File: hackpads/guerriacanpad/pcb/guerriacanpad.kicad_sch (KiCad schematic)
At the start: 53 parts, among them SW1 RotaryEncoder_Switch_MP, SW2 RotaryEncoder_Switch_MP, U1 Seeeduino Xiao rp2040, U2 MCP23008-xSO, U3 74AHC1G125

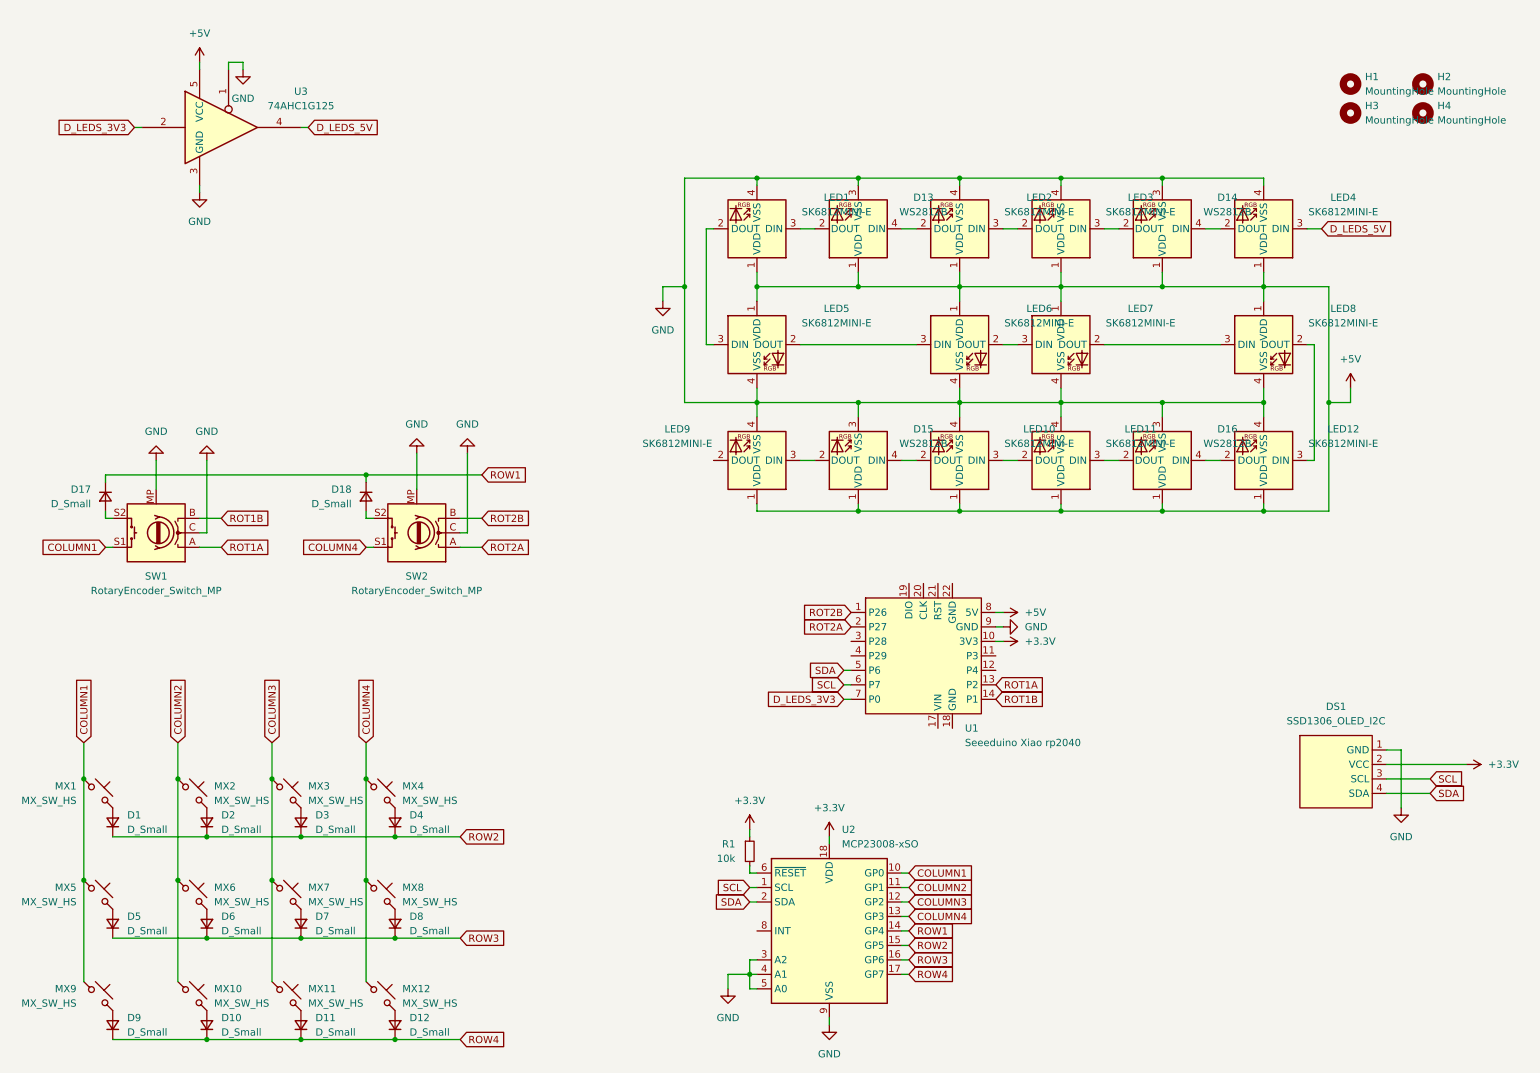
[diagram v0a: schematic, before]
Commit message: Changed the IO expander
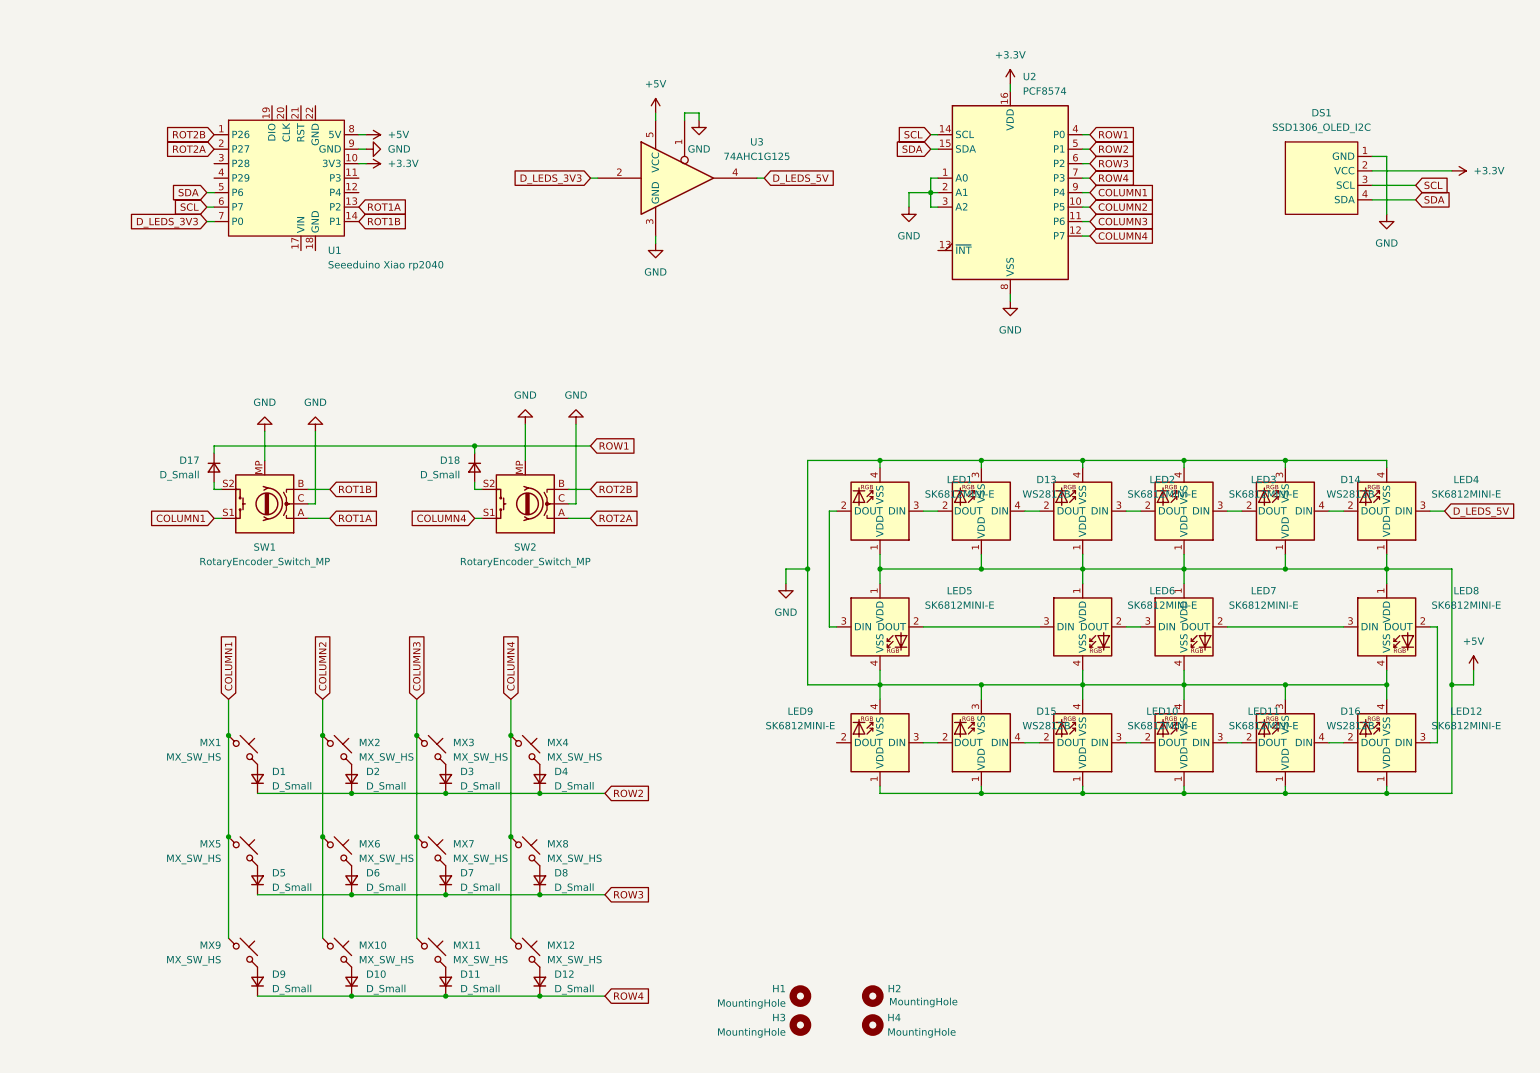
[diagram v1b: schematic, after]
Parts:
- removed R1: 10k, Resistor_SMD:R_0603_1608Metric_Pad0.98x0.95mm_HandSolder, symbol Device:R_Small
- removed U2: MCP23008-xSO, Package_SO:SOIC-18W_7.5x11.6mm_P1.27mm, symbol Interface_Expansion:MCP23008-xSO
- added U2: PCF8574, Package_SO:SOIC-16W_7.5x10.3mm_P1.27mm, symbol Interface_Expansion:PCF8574
- U3: footprint Package_TO_SOT_SMD:SOT-23-5_HandSoldering -> Package_TO_SOT_SMD:SOT-353_SC-70-5_Handsoldering
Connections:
- net +3.3V: now also U2.16 (VDD)
- net COLUMN1: now also U2.9 (P4)
- net COLUMN2: now also U2.10 (P5)
- net COLUMN3: now also U2.11 (P6)
- net COLUMN4: now also U2.12 (P7)
- net GND: now also U2.1 (A0), U2.2 (A1), U2.3 (A2), U2.8 (VSS)
- net ROW1: now also U2.4 (P0)
- net ROW2: now also U2.5 (P1)
- net ROW3: now also U2.6 (P2)
- net ROW4: now also U2.7 (P3)
- net SCL: now also U2.14 (SCL)
- net SDA: now also U2.15 (SDA)
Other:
- moved on the sheet: D1, D10, D11, D12, D13, D14, D15, D16, D17, D18, D2, D3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

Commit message: Added decoupling capacitors
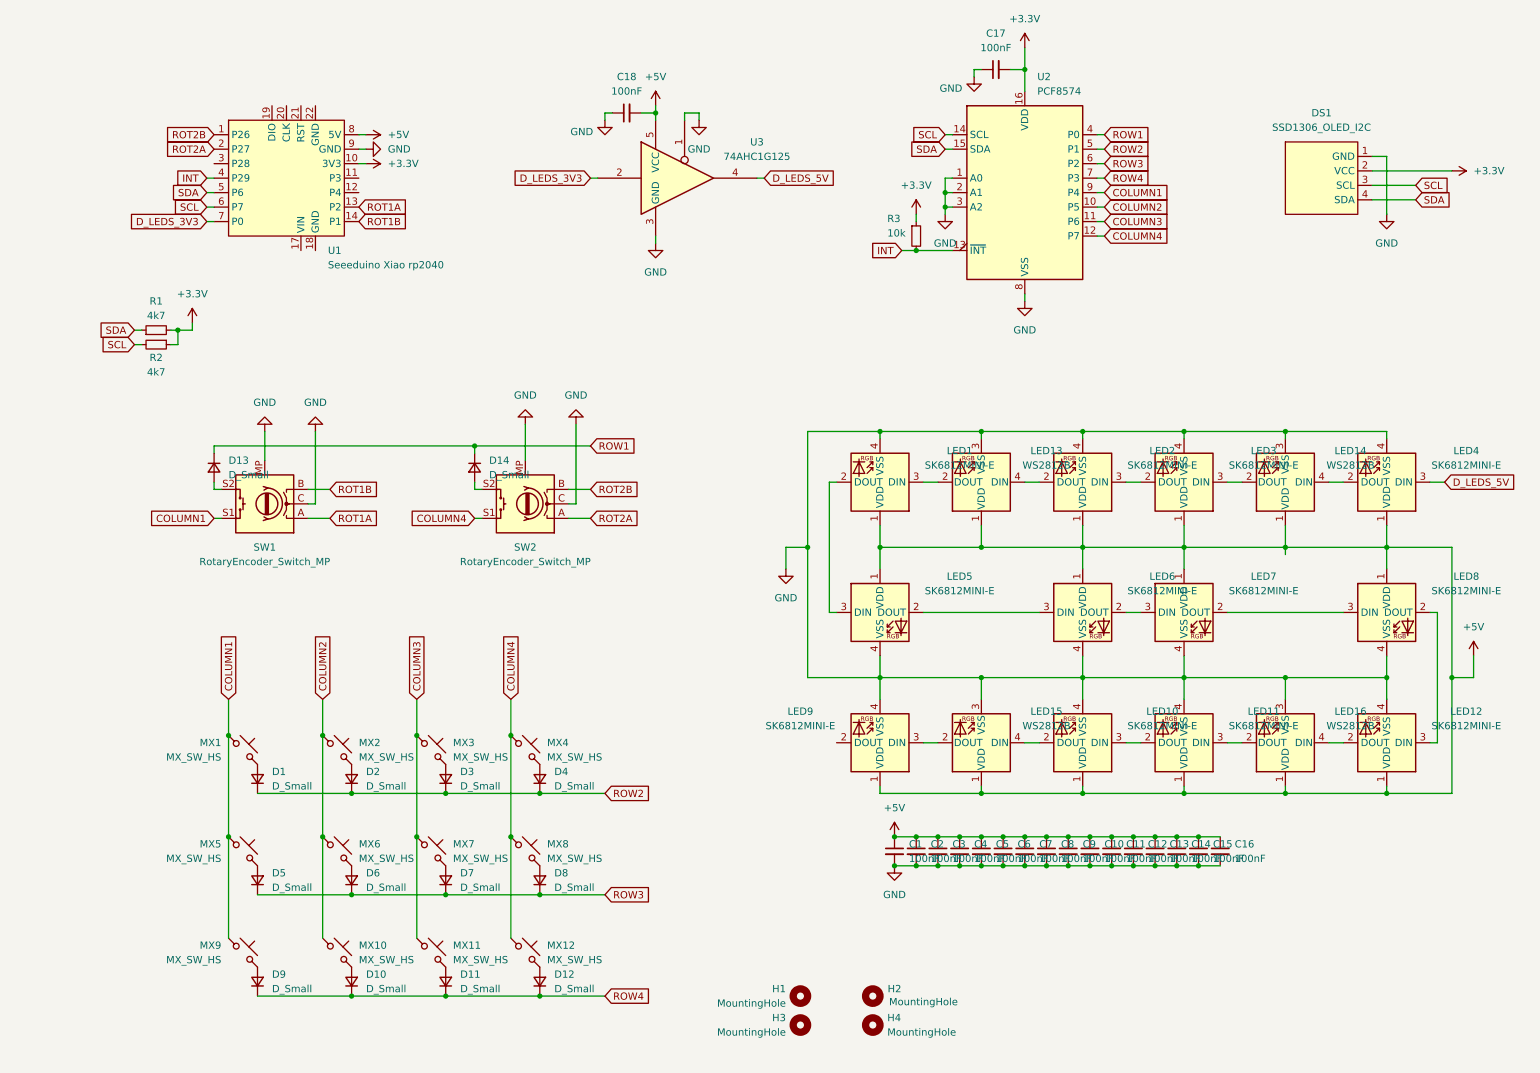
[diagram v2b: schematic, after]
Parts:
- added C1, C10, C11, C12, C13, C14, C15, C16, C17, C18, C2, C3, C4, C5, C6, C7, C8, C9: 100nF, Capacitor_SMD:C_0603_1608Metric_Pad1.08x0.95mm_HandSolder, symbol Device:C_Small
- added R1, R2: 4k7, Resistor_SMD:R_0603_1608Metric_Pad0.98x0.95mm_HandSolder, symbol Device:R_Small
- added R3: 10k, Resistor_SMD:R_0603_1608Metric_Pad0.98x0.95mm_HandSolder, symbol Device:R_Small
- renumbered D17 to D13, D18 to D14, D13 to LED13, D14 to LED14, D15 to LED15, D16 to LED16
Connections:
- net +3.3V: now also C17.2, R1.2, R2.1, R3.1
- net +5V: now also C1.1, C10.1, C11.1, C12.1, C13.1, C14.1, C15.1, C16.1, C18.2, C2.1, C3.1, C4.1, C5.1, C6.1, C7.1, C8.1, C9.1
- net GND: now also C1.2, C10.2, C11.2, C12.2, C13.2, C14.2, C15.2, C16.2, C17.1, C18.1, C2.2, C3.2, C4.2, C5.2, C6.2, C7.2, C8.2, C9.2
- net SCL: now also R2.2
- net SDA: now also R1.1
- net INT: now reaches U2.13 (~{INT})
- net INT: now also U1.4 (P29), R3.2
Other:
- moved on the sheet: LED1, LED13, LED14, LED2, LED3, LED4, LED5, LED6, LED7, LED8, U2
